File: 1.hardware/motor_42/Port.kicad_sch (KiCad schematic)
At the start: 17 parts, among them J1 PC_CONN, J11 WAGO_2060, J12 WAGO_2060, J2 MT6816_CONN, J4 DEBUG, J5 CAN_IN, J6 CAN_OUT, J7 ESP_DOWNLOAD, J9 WS2812_OUT, U3 SN65HVD232

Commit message: 중간 저장
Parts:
- TP1, TP2, TP3, TP4: value PAD_4_15 -> PAD_4_12; footprint New_Footprints:custom_pad_4_15 -> New_Footprints:custom_pad_2_5
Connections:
- net OUT_A+: now also TP2.1; no longer TP1.1
- net OUT_A-: now also TP1.1; no longer TP2.1
- net OUT_B+: now also TP4.1; no longer TP3.1
- net OUT_B-: now also TP3.1; no longer TP4.1
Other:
- moved on the sheet: TP1, TP2, TP3, TP4

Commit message: 얼추 다 그림
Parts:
- removed J9: WS2812_OUT, Connector_JST:JST_SH_SM03B-SRSS-TB_1x03-1MP_P1.00mm_Horizontal, symbol Connector_Generic:Conn_01x03
- removed R39: 4.7k/0.063w, Resistor_SMD:R_0402_1005Metric, symbol Device:R_Small_US

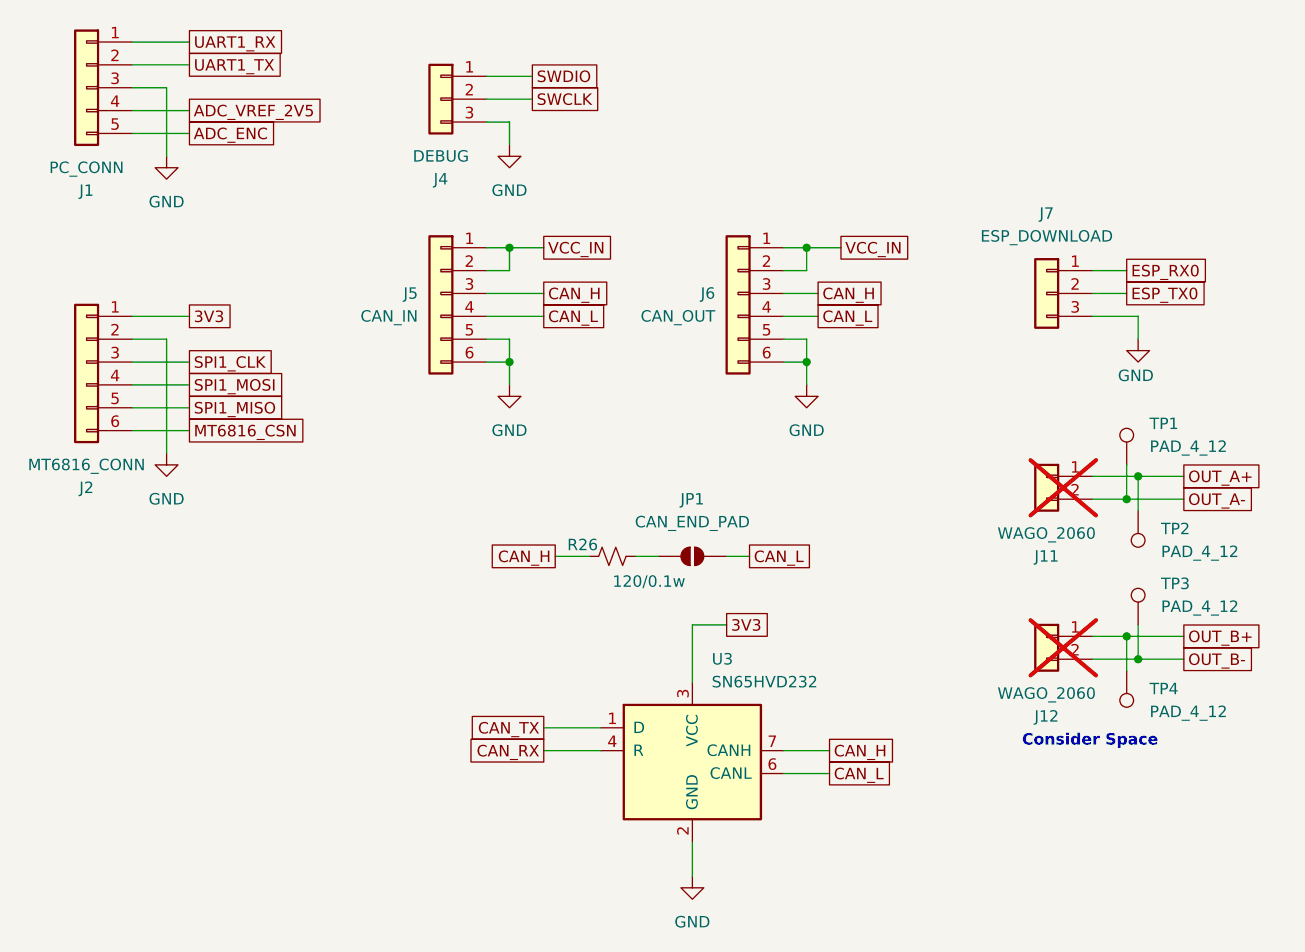
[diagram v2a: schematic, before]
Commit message: 번호 초기화 및 led 변경
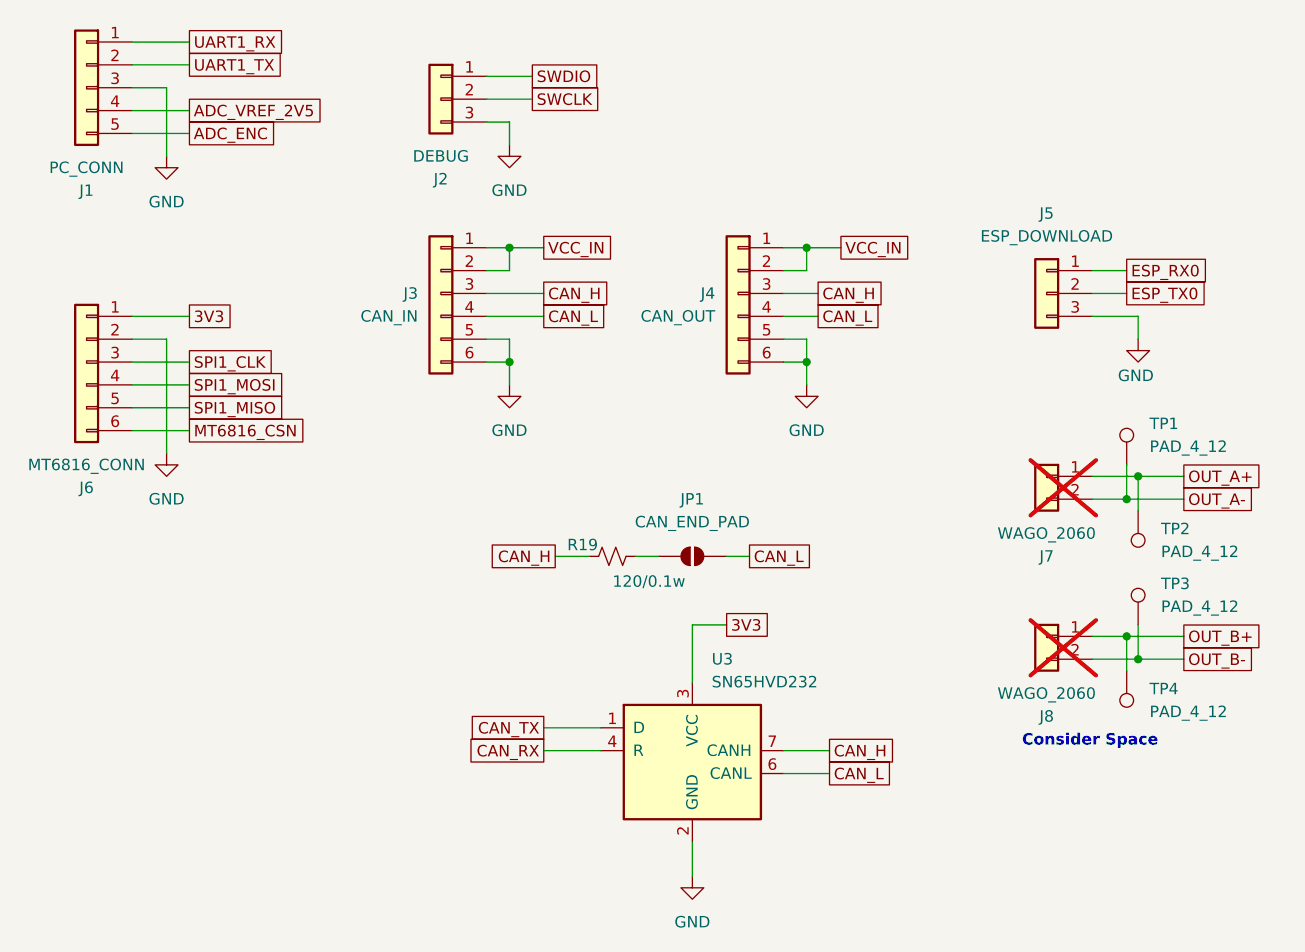
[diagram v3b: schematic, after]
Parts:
- renumbered J4 to J2, J5 to J3, J6 to J4, J7 to J5, J2 to J6, J11 to J7, J12 to J8, R26 to R19
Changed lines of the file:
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@@
 		(on_board yes)
 		(dnp no)
-		(property "Reference" "J5"
+		(property "Reference" "J3"
 			(at 69.85 50.7999 0)
 			(effects
@@
 			(project ""
 				(path "/3c5de6a8-6840-43a5-a2fb-24dbb7f0450d/a6d4f9ac-ce94-4e25-ac55-8dc736c58565"
-					(reference "J5")
+					(reference "J3")
 					(unit 1)
 				)
@@
 		(on_board yes)
 		(dnp no)
-		(property "Reference" "J2"
+		(property "Reference" "J6"
 			(at 33.02 72.39 0)
 			(effects
@@
 			(project ""
 				(path "/3c5de6a8-6840-43a5-a2fb-24dbb7f0450d/a6d4f9ac-ce94-4e25-ac55-8dc736c58565"
-					(reference "J2")
+					(reference "J6")
 					(unit 1)
 				)
@@
 		(dnp no)
 		(fields_autoplaced yes)
-		(property "Reference" "#PWR043"
+		(property "Reference" "#PWR038"
 			(at 100.33 121.92 0)
 			(effects
@@
 			(project "motor_42"
 				(path "/3c5de6a8-6840-43a5-a2fb-24dbb7f0450d/a6d4f9ac-ce94-4e25-ac55-8dc736c58565"
-					(reference "#PWR043")
+					(reference "#PWR038")
 					(unit 1)
 				)
@@
 		(dnp no)
 		(fields_autoplaced yes)
-		(property "Reference" "J7"
+		(property "Reference" "J5"
 			(at 139.7 41.91 0)
 			(effects
@@
 			(project "motor_42"
 				(path "/3c5de6a8-6840-43a5-a2fb-24dbb7f0450d/a6d4f9ac-ce94-4e25-ac55-8dc736c58565"
-					(reference "J7")
+					(reference "J5")
 					(unit 1)
 				)
@@
 		(on_board yes)
 		(dnp no)
-		(property "Reference" "#PWR045"
+		(property "Reference" "#PWR034"
 			(at 149.86 62.23 0)
 			(effects
@@
 			(project "motor_42"
 				(path "/3c5de6a8-6840-43a5-a2fb-24dbb7f0450d/a6d4f9ac-ce94-4e25-ac55-8dc736c58565"
-					(reference "#PWR045")
+					(reference "#PWR034")
 					(unit 1)
 				)
@@
 		(dnp no)
 		(fields_autoplaced yes)
-		(property "Reference" "#PWR035"
+		(property "Reference" "#PWR037"
 			(at 41.91 74.93 0)
 			(effects
@@
 			(project "motor_42"
 				(path "/3c5de6a8-6840-43a5-a2fb-24dbb7f0450d/a6d4f9ac-ce94-4e25-ac55-8dc736c58565"
-					(reference "#PWR035")
+					(reference "#PWR037")
 					(unit 1)
 				)
@@
 		(on_board no)
 		(dnp yes)
-		(property "Reference" "J12"
+		(property "Reference" "J8"
 			(at 139.7 97.79 0)
 			(effects
@@
 			(project "motor_42"
 				(path "/3c5de6a8-6840-43a5-a2fb-24dbb7f0450d/a6d4f9ac-ce94-4e25-ac55-8dc736c58565"
-					(reference "J12")
+					(reference "J8")
 					(unit 1)
 				)
@@
 		(dnp no)
 		(fields_autoplaced yes)
-		(property "Reference" "#PWR041"
+		(property "Reference" "#PWR035"
 			(at 80.01 67.31 0)
 			(effects
@@
 			(project "motor_42"
 				(path "/3c5de6a8-6840-43a5-a2fb-24dbb7f0450d/a6d4f9ac-ce94-4e25-ac55-8dc736c58565"
-					(reference "#PWR041")
+					(reference "#PWR035")
 					(unit 1)
 				)
@@
 		(dnp no)
 		(fields_autoplaced yes)
-		(property "Reference" "#PWR044"
+		(property "Reference" "#PWR036"
 			(at 113.03 67.31 0)
 			(effects
@@
 			(project "motor_42"
 				(path "/3c5de6a8-6840-43a5-a2fb-24dbb7f0450d/a6d4f9ac-ce94-4e25-ac55-8dc736c58565"
-					(reference "#PWR044")
+					(reference "#PWR036")
 					(unit 1)
 				)
@@
 		(on_board yes)
 		(dnp no)
-		(property "Reference" "R26"
+		(property "Reference" "R19"
 			(at 88.138 78.74 90)
 			(effects
@@
 			(project "motor_42"
 				(path "/3c5de6a8-6840-43a5-a2fb-24dbb7f0450d/a6d4f9ac-ce94-4e25-ac55-8dc736c58565"
-					(reference "R26")
+					(reference "R19")
 					(unit 1)
 				)
@@
 		(on_board no)
 		(dnp yes)
-		(property "Reference" "J11"
+		(property "Reference" "J7"
 			(at 139.7 80.01 0)
 			(effects
@@
 			(project ""
 				(path "/3c5de6a8-6840-43a5-a2fb-24dbb7f0450d/a6d4f9ac-ce94-4e25-ac55-8dc736c58565"
-					(reference "J11")
+					(reference "J7")
 					(unit 1)
 				)
@@
 		(dnp no)
 		(fields_autoplaced yes)
-		(property "Reference" "#PWR040"
+		(property "Reference" "#PWR032"
 			(at 80.01 40.64 0)
 			(effects
@@
 			(project "motor_42"
 				(path "/3c5de6a8-6840-43a5-a2fb-24dbb7f0450d/a6d4f9ac-ce94-4e25-ac55-8dc736c58565"
-					(reference "#PWR040")
+					(reference "#PWR032")
 					(unit 1)
 				)
@@
 		(on_board yes)
 		(dnp no)
-		(property "Reference" "J6"
+		(property "Reference" "J4"
 			(at 102.87 50.7999 0)
 			(effects
@@
 			(project "motor_42"
 				(path "/3c5de6a8-6840-43a5-a2fb-24dbb7f0450d/a6d4f9ac-ce94-4e25-ac55-8dc736c58565"
-					(reference "J6")
+					(reference "J4")
 					(unit 1)
 				)
@@
 		(dnp no)
 		(fields_autoplaced yes)
-		(property "Reference" "#PWR034"
+		(property "Reference" "#PWR033"
 			(at 41.91 41.91 0)
 			(effects
@@
 			(project "motor_42"
 				(path "/3c5de6a8-6840-43a5-a2fb-24dbb7f0450d/a6d4f9ac-ce94-4e25-ac55-8dc736c58565"
-					(reference "#PWR034")
+					(reference "#PWR033")
 					(unit 1)
 				)
@@
 		(on_board yes)
 		(dnp no)
-		(property "Reference" "J4"
+		(property "Reference" "J2"
 			(at 72.39 38.1 0)
 			(effects
@@
 			(project ""
 				(path "/3c5de6a8-6840-43a5-a2fb-24dbb7f0450d/a6d4f9ac-ce94-4e25-ac55-8dc736c58565"
-					(reference "J4")
-					(unit 1)
-				)
+					(reference "J2")
+					(unit 1)
+				)
